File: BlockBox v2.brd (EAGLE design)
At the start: 199.4 x 119 mm, 367 parts, among them J100 TE-770966, J400 ICSP, J401 LED, J402 SWLED, J403 USB1, J404 USB2, J405 ZX62D-B-5PA8, J406 ZX62D-B-5PA8, J407 ZX62D-B-5PA8, J408 AUX, Q100 TK3R1E04PL, Q101 TK3R1E04PL, Q102 IPP052N06L3 G, Q103 IPP052N06L3 G, Q104 IPP052N06L3 G, Q105 IPP052N06L3 G, Q106 TK3R1E04PL, Q200 SUP90142E-GE3, Q201 SUP90142E-GE3, Q202 BUK9Y43-60E, Q203 DMP4065S, Q400 DMG2302UK, Q401 DMG2302UK, Q402 DMG2302UK, Q403 DMG2302UK, Q404 NMOS, Q405 NMOS, Q406 NMOS, SW100 PWRSW, SW400 VOL-, SW401 MFB, SW402 VOL+, SW403 BACK, SW404 PLAY, SW405 FWD, SW406 LCD_BL, SW407 LEDMODE, SW408 SDA01H1S, SW409 RESET, U100 BQ77915, U101 MAX1737, U102 LM74700-Q1, U103 LM74700-Q1, U104 LM74700-Q1, U200 LM5022, U201 LM3488, U202 LM25085, U203 TPS54308, U204 LD39150DT33, U300 TAS5548, U301 TAS5634, U302 NCS20071, U400 PIC32MZ-EF-100-I/PF, U401 FT230XS, U402 NCS4333, U403 FSAL200MTC, Y300 12.288MHz, Y400 12MHz

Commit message: Major PCB progress, about to shrink PCB (safety commit)
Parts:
- removed TP325, TP326: TPTP15R, testpad:TP15R
- moved U104 601.6 mm to (139.7, 2.54), flipped to the bottom, turned to 90 degrees
- moved U103 585.1 mm to (139.7, 14.0), flipped to the bottom, turned to 90 degrees
- moved TP102 579.4 mm to (96.5, -61.0)
- moved TP104 578.3 mm to (81.3, -61.0)
- moved TP105 578.3 mm to (74.9, -61.0)
- moved TP106 578.3 mm to (68.6, -61.0)
- moved R101 548.2 mm to (64.3, 14.0), flipped to the bottom, turned to 180 degrees
- moved D100 546.3 mm to (117.6, 13.6), turned to 270 degrees
- moved D102 544.5 mm to (83.8, 22.2), flipped to the bottom, turned to 180 degrees
- moved D101 544.0 mm to (112.0, 18.3), flipped to the bottom
- moved R127 543.0 mm to (92.8, 10.4), turned to 90 degrees
- moved R100 542.5 mm to (66.2, 18.0), flipped to the bottom, turned to 180 degrees
- moved R111 541.6 mm to (85.3, 14.5), turned to 180 degrees
- moved R107 540.1 mm to (72.8, 7.24), turned to 90 degrees
- moved R108 538.2 mm to (82.5, 11.4), turned to 90 degrees
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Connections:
- net AMP_!CLIP: now also TP310.TP; no longer TP326.TP
- net AMP_!OTW: now also TP309.TP; no longer TP325.TP
- net AMP_AVDD: no longer TP310.TP
- net AMP_DVDD: no longer TP309.TP
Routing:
- net VBAT: track 0.00 -> 160.8 mm, vias 0 -> 3
- net AMP_PVDD: track 0.00 -> 90.5 mm
- net CHG_CSSP: track 0.00 -> 81.6 mm, vias 0 -> 2
- net VSUP: track 0.00 -> 78.6 mm, vias 0 -> 2
- net VIN_EXT_FUSED: track 0.00 -> 73.8 mm, vias 0 -> 1
- net BAT-: track 0.00 -> 64.6 mm, vias 0 -> 9
- net CHG_CSSN: track 0.00 -> 64.2 mm, vias 0 -> 1
- net CHG_LX: track 0.00 -> 52.9 mm, vias 0 -> 1
- net BOOST_SW_DRAIN: track 0.00 -> 44.5 mm
- net 12V: track 0.00 -> 39.0 mm, vias 0 -> 1
- net CHG_!SHDN: track 0.00 -> 35.5 mm, vias 0 -> 1
- net BOOST_SW_GATE: track 0.00 -> 32.6 mm
- net DSP_XTALI: track 0.00 -> 28.7 mm
- net CHG_CS: track 0.00 -> 27.8 mm, vias 0 -> 3
- net BAT_THERM: track 0.00 -> 25.3 mm, vias 0 -> 2
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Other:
- board size 199.4 x 119 mm -> 141 x 119 mm

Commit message: Voltage converter layout done
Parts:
- moved R216 312.0 mm to (67.9, 40.3), flipped to the bottom
- moved R219 308.3 mm to (63.9, 41.5), flipped to the bottom, turned to 90 degrees
- moved U202 306.8 mm to (71.1, 40.6), flipped to the bottom, turned to 270 degrees
- moved C218 294.4 mm to (55.0, 31.9), turned to 270 degrees
- moved U203 294.4 mm to (66.2, 51.8), flipped to the bottom, turned to 270 degrees
- moved C215 288.0 mm to (67.9, 38.2), flipped to the bottom, turned to 180 degrees
- moved TP201 286.9 mm to (31.0, 79.4)
- moved C217 280.9 mm to (61.3, 40.4), flipped to the bottom, turned to 180 degrees
- moved R215 280.3 mm to (67.9, 44.3), flipped to the bottom
- moved C216 279.9 mm to (67.9, 42.3), flipped to the bottom, turned to 180 degrees
- moved U204 279.8 mm to (70.1, 50.4), turned to 270 degrees
- moved TP202 275.7 mm to (55.4, 36.6)
- moved L202 271.9 mm to (63.4, 39.9), turned to 180 degrees
- moved TP203 259.7 mm to (56.0, 58.0)
- moved C228 257.4 mm to (61.7, 60.2), flipped to the bottom, turned to 180 degrees
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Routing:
- net VSUP: track 78.6 -> 188.5 mm, vias 2 -> 6
- net 12V: track 39.0 -> 101.4 mm
- net 3.6V: track 0.00 -> 20.1 mm
- net SEPIC_SW_DRAIN: track 0.00 -> 18.9 mm, vias 0 -> 1
- net BUCK_FB: track 0.00 -> 17.7 mm, vias 0 -> 2
- net 5V: track 0.00 -> 16.4 mm, vias 0 -> 1
- net SEPIC_PREDIODE: track 0.00 -> 14.8 mm, vias 0 -> 1
- net SEPIC_SW_SOURCE: track 0.00 -> 13.9 mm, vias 0 -> 1
- net BUCK_SW_SOURCE: track 0.00 -> 9.32 mm
- net 3.3V: track 10.1 -> 18.7 mm
- net PRELIN_SW: track 0.00 -> 7.69 mm
- net SEPIC_COMP: track 0.00 -> 6.83 mm
- net SEPIC_FB: track 0.00 -> 6.07 mm
- net BUCK_SW_DRAIN: track 0.00 -> 5.70 mm, vias 0 -> 2
- net AMP_PVDD: track 90.5 -> 84.9 mm
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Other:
- board size 141 x 119 mm -> 124.5 x 119 mm

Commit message: PCB initially completed, final fixes
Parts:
- removed C417, C418, C419, C420: 0.1µF, rcl:C0603
- removed C421, C422: 18pF, rcl:C0603
- removed D401, D402, D403, D404: BAT60A, BW-Active:SOD323
- removed J407: ZX62D-B-5PA8, BW-Connectors:ZX62D-B-5PA8
- removed SJ403: FTRESET, jumper:SJ
- removed SJ404: USB-5V, jumper:SJ_2
- removed TP322, TP323, TP324, TP401, TP402, TP403, TP404, TP405, TP406, TP407: TPTP15R, testpad:TP15R
- added R411, R412: 10kΩ, resistor:R0603
- added R413, R414: 1kΩ, resistor:R0603
- added U404: NCS2333, BW-Active:MSOP8
- C401, C402, C403, C404, C407: value 15pF -> 0.1µF
- C405, C406: value 15pF -> 18pF
- SJ400: value USB -> USB-5V
- U400: value PIC32MZ-EF-100-I/PF -> PIC32MZ-EF-100
- U402: value NCS4333 -> NCS2333; device BW-Active:SO14 -> BW-Active:MSOP8
- moved R406 291.5 mm to (46.6, 59.2), turned to 180 degrees
- moved C411 284.0 mm to (41.4, 53.0), flipped to the bottom, turned to 270 degrees
- moved TP409 282.7 mm to (46.2, 45.5)
- moved TP411 279.8 mm to (24.3, 62.1), turned to 90 degrees
- moved C410 278.7 mm to (41.4, 49.9), flipped to the bottom, turned to 90 degrees
- moved TP408 274.5 mm to (43.7, 45.6)
- moved RV401 274.3 mm to (53.3, 41.1), turned to 180 degrees
- moved C407 271.7 mm to (49.5, 48.9), flipped to the bottom, turned to 270 degrees
- moved TP412 270.1 mm to (24.3, 56.1), turned to 90 degrees
- moved Q405 269.6 mm to (36.7, 28.7), flipped to the bottom
- moved SJ402 269.3 mm to (21.2, 68.3), flipped to the bottom, turned to 180 degrees
- moved SJ401 267.4 mm to (26.8, 35.2)
- moved R404 267.3 mm to (12.8, 23.6), flipped to the bottom, turned to 180 degrees
- moved C409 267.1 mm to (35.6, 49.5), flipped to the bottom
- moved Q404 266.1 mm to (40.8, 28.7), flipped to the bottom
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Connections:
- removed net BAT_CSN_BUF: R409.2, U402.8, U402.9
- removed net BAT_CSP_BUF: R408.2, U402.13, U402.14
- removed net FT_!RESET: SJ403.2, U401.11
- removed net MCU_USBID: J407.4, U400.56
- removed net MCU_USB_D+: J407.3, U400.55
- removed net MCU_USB_D-: J407.2, U400.54
- removed net MCU_USB_VBUS: J407.1, U400.51
- removed net MCU_VUSB3V3: SJ400.2, U400.52
- new net MCU_BAT_SENSE_BUF: C404.1, TP408.TP, U400.26, U404.6, U404.7
- new net MCU_BAT_SENSE_FB: R411.1, U402.1, U402.2
- new net MCU_CURR_SENSE_BUF: C403.1, TP409.TP, U400.27, U404.1, U404.2
- new net MCU_CURR_SENSE_FB: R407.1, R412.2, U402.7
- net 3.3V: now also C401.1, C402.1, C407.1, R413.2, R414.2, U402.8, U404.8; no longer C417.1, C418.1, C419.1, C420.1, D401.1, D402.1, SJ400.1, U402.4
- net 5V: now also SJ400.3; no longer SJ404.3
- net AMP_!CLIP: no longer TP310.TP
- net AMP_!FAULT: no longer TP324.TP
- net AMP_!OTW: no longer TP309.TP
- net AMP_!RESET: now also TP321.TP; no longer TP323.TP
- net BAT-: now also C402.2, U402.4; no longer U402.11
- net BAT_CSN: now also R409.2; no longer U402.10
- net BAT_CSP: now also R408.2; no longer U402.12
- net BM_ADAP_IN: now also SJ400.2; no longer SJ404.2
- net BM_USB_VBUS: now also SJ400.1; no longer SJ404.1
- net DSP_!BKND_ERR: now also TP310.TP; no longer TP322.TP
- net DSP_SCL: now also R414.1
- net DSP_SDA: now also R413.1
- net DSP_VALID: now also TP309.TP; no longer TP321.TP
- net GND: now also C401.2, C403.2, C404.2, C407.2, U400.52, U404.4; no longer C401.1, C402.1, C403.1, C404.1, C407.1, C417.2, C418.2, C419.2, C420.2, C421.1, C422.1, D403.2, D404.2, J407.5, J407.S1, J407.S2, J407.S3, J407.S4, SJ400.3, SJ403.1
- net LCD_!CS: no longer TP404.TP
- net LCD_!INT: no longer TP406.TP
- net LCD_!PD: no longer TP405.TP
- net LCD_BL_CTL: no longer TP407.TP
- net LCD_MISO: no longer TP402.TP
- net LCD_MOSI: no longer TP403.TP
- net LCD_SCK: no longer TP401.TP
- net MCU_BACK_SW: no longer C404.2
- net MCU_BAT_SENSE: now also R411.2, U404.5; no longer D401.2, D403.1, TP408.TP, U400.26, U402.1, U402.2
- net MCU_CURR_SENSE: now also R412.1, U404.3; no longer D402.2, D404.1, R407.1, TP409.TP, U400.27, U402.7
- net MCU_FWD_SW: no longer C402.2
- net MCU_LCD_BL_SW: no longer C401.2
- net MCU_MFB_SW: no longer C406.2
- net MCU_OSC1: now also C405.2; no longer C421.2
- net MCU_OSC2_R: now also C406.2; no longer C422.2
- net MCU_PLAY_SW: no longer C403.2
- net MCU_VOL+_SW: no longer C405.2
- net MCU_VOL-_SW: no longer C407.2
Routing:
- net 3.3V: track 18.7 -> 330.6 mm, vias 3 -> 19
- net 5V: track 16.4 -> 128.2 mm, vias 1 -> 3
- net I2S_LRCLK: track 0.00 -> 95.6 mm, vias 0 -> 4
- net I2S_SCLK: track 0.00 -> 91.6 mm, vias 0 -> 4
- net I2S_SD: track 0.00 -> 87.8 mm, vias 0 -> 5
- net 12V: track 101.4 -> 182.6 mm, vias 1 -> 3
- net MCU_!MCLR: track 0.00 -> 76.3 mm, vias 0 -> 4
- net MCU_CURR_SENSE: track 0.00 -> 75.5 mm
- net MCU_BAT_SENSE: track 0.00 -> 74.6 mm
- net MCU_PGD: track 0.00 -> 70.3 mm, vias 0 -> 4
- net MCU_PGC: track 0.00 -> 68.9 mm, vias 0 -> 4
- net DSP_EMO1: track 0.00 -> 64.5 mm
- net DSP_!RESET: track 0.00 -> 62.8 mm
- net DSP_!PDN: track 0.00 -> 61.3 mm
- net DSP_!BKND_ERR: track 0.00 -> 61.3 mm
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- added copper zone on layer 1, net GND
- added copper zone on layer 16, net GND
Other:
- board text added: "+"
- board text added: "-"
- board text added: "2"
- board text added: "<"
- board text added: ">"
- board text added: "BM83"
- board text added: "G"
- board text added: "LCD"
- board text added: "M"
- board text added: "MCU-USB"
- board text added: "POT"
- board text added: "UART"
- board text added: "USB"
- board text added: "||"

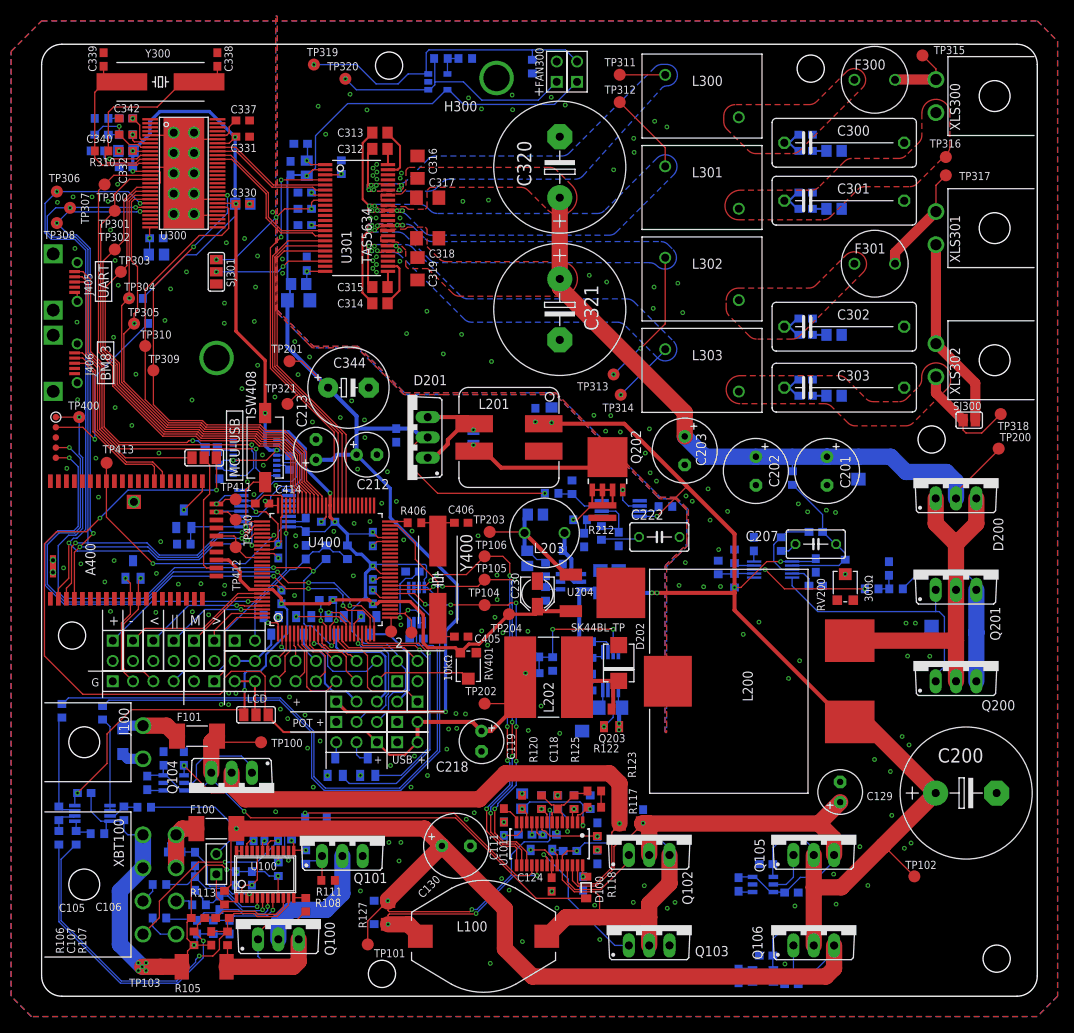
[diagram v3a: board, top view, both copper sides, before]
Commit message: Added logo and ground TPs
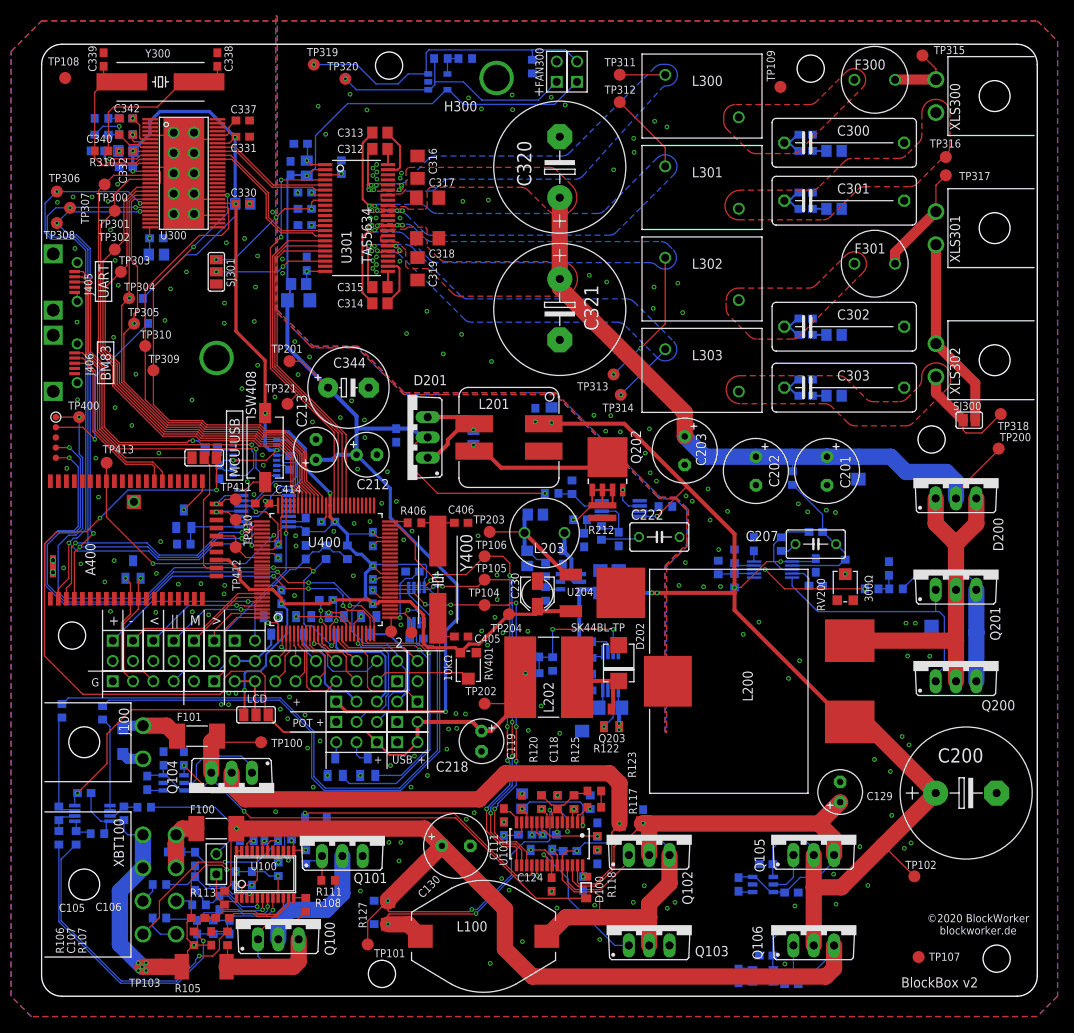
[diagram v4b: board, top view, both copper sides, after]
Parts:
- added TP107, TP108, TP109: TPTP15R, testpad:TP15R
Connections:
- net GND: now also TP107.TP, TP108.TP, TP109.TP
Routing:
- net GND: vias 247 -> 248
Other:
- board text added: "BlockBox v2"
- board text added: "©2020 BlockWorker blockworker.de"
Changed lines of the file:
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@@
 <wire x1="29.3624" y1="100.5586" x2="29.3624" y2="98.4758" width="0.8128" layer="29"/>
 <wire x1="30.099" y1="84.963" x2="33.909" y2="81.153" width="0.8128" layer="29"/>
-<wire x1="33.909" y1="81.153" x2="39.497" y2="81.153" width="0.8128" layer="29"/>
-<wire x1="39.497" y1="81.153" x2="45.3136" y2="75.3364" width="0.8128" layer="29"/>
-<wire x1="45.3136" y1="75.3364" x2="64.2366" y2="75.3364" width="0.8128" layer="29"/>
-<wire x1="64.2366" y1="75.3364" x2="67.2338" y2="72.3392" width="0.8128" layer="29"/>
 <wire x1="68.8848" y1="70.6882" x2="68.9102" y2="70.6628" width="0.8128" layer="29"/>
 <wire x1="74.1934" y1="65.3796" x2="77.2922" y2="62.2808" width="0.8128" layer="29"/>
 <wire x1="77.2922" y1="62.2808" x2="78.2828" y2="62.2808" width="0.8128" layer="29"/>
 <wire x1="79.6798" y1="61.8744" x2="80.7466" y2="60.8076" width="0.8128" layer="29"/>
-<wire x1="80.7466" y1="60.8076" x2="80.7466" y2="58.3438" width="0.8128" layer="29"/>
-<wire x1="80.6958" y1="56.4134" x2="78.0288" y2="53.7464" width="0.8128" layer="29"/>
 <wire x1="78.0288" y1="53.7464" x2="78.0288" y2="51.2318" width="0.8128" layer="29"/>
 <wire x1="78.0288" y1="49.6316" x2="78.0288" y2="43.2308" width="0.8128" layer="29"/>
 <wire x1="78.0288" y1="35.56" x2="78.0288" y2="33.1978" width="0.8128" layer="29"/>
 <wire x1="29.3624" y1="118.999" x2="29.3624" y2="102.6922" width="0.8128" layer="30"/>
-<wire x1="29.3624" y1="101.4984" x2="29.3624" y2="98.4758" width="0.8128" layer="30"/>
 <wire x1="29.3624" y1="94.0562" x2="29.3624" y2="91.5924" width="0.8128" layer="30"/>
 <wire x1="29.3624" y1="89.916" x2="29.3624" y2="88.4428" width="0.8128" layer="30"/>
@@
 <wire x1="8.763" y1="91.821" x2="6.731" y2="91.821" width="0.1524" layer="21"/>
 <text x="62.738" y="112.395" size="1.27" layer="21" font="vector" ratio="15" rot="R90">+</text>
+<polygon width="0.1524" layer="29">
+<vertex x="113.284" y="15.5702"/>
+<vertex x="116.332" y="15.5702"/>
+<vertex x="116.713" y="15.1892"/>
+<vertex x="116.713" y="13.6652"/>
+<vertex x="115.57" y="13.6652"/>
+<vertex x="115.951" y="14.0462"/>
+<vertex x="115.951" y="14.4272"/>
+<vertex x="115.57" y="14.8082"/>
+<vertex x="114.046" y="14.8082"/>
+<vertex x="114.046" y="10.9982"/>
+<vertex x="113.284" y="10.9982"/>
+</polygon>
+<polygon width="0.1524" layer="29">
+<vertex x="114.046" y="10.9982"/>
+<vertex x="116.332" y="10.9982"/>
+<vertex x="116.713" y="11.3792"/>
+<vertex x="116.713" y="12.9032"/>
+<vertex x="116.332" y="13.2842"/>
+<vertex x="116.713" y="13.6652"/>
+<vertex x="114.046" y="13.6652"/>
+<vertex x="114.046" y="12.9032"/>
+<vertex x="115.57" y="12.9032"/>
+<vertex x="115.951" y="12.5222"/>
+<vertex x="115.951" y="12.1412"/>
+<vertex x="115.57" y="11.7602"/>
+<vertex x="114.046" y="11.7602"/>
+</polygon>
+<polygon width="0.1524" layer="29">
+<vertex x="117.475" y="11.3792"/>
+<vertex x="117.856" y="10.9982"/>
+<vertex x="118.999" y="10.9982"/>
+<vertex x="119.38" y="11.3792"/>
+<vertex x="119.761" y="10.9982"/>
+<vertex x="120.904" y="10.9982"/>
+<vertex x="121.285" y="11.3792"/>
+<vertex x="121.285" y="15.1892"/>
+<vertex x="120.904" y="15.5702"/>
+<vertex x="120.523" y="15.5702"/>
+<vertex x="120.523" y="12.5222"/>
+<vertex x="120.142" y="12.1412"/>
+<vertex x="119.761" y="12.5222"/>
+<vertex x="119.761" y="15.1892"/>
+<vertex x="119.38" y="15.5702"/>
+<vertex x="118.999" y="15.1892"/>
+<vertex x="118.999" y="12.5222"/>
+<vertex x="118.618" y="12.1412"/>
+<vertex x="118.237" y="12.5222"/>
+<vertex x="118.237" y="15.5702"/>
+<vertex x="117.856" y="15.5702"/>
+<vertex x="117.475" y="15.1892"/>
+</polygon>
+<wire x1="113.284" y1="15.9512" x2="112.903" y2="15.5702" width="0.1524" layer="29"/>
+<wire x1="112.903" y1="15.5702" x2="112.903" y2="10.9982" width="0.1524" layer="29"/>
+<wire x1="112.903" y1="10.9982" x2="113.284" y2="10.6172" width="0.1524" layer="29"/>
+<wire x1="113.284" y1="10.6172" x2="121.285" y2="10.6172" width="0.1524" layer="29"/>
+<wire x1="121.285" y1="10.6172" x2="121.666" y2="10.9982" width="0.1524" layer="29"/>
+<wire x1="121.666" y1="10.9982" x2="121.666" y2="15.5702" width="0.1524" layer="29"/>
+<wire x1="121.666" y1="15.5702" x2="121.285" y2="15.9512" width="0.1524" layer="29"/>
+<wire x1="121.285" y1="15.9512" x2="113.284" y2="15.9512" width="0.1524" layer="29"/>
+<text x="117.0686" y="7.7216" size="1.016" layer="21" font="vector" ratio="15" align="bottom-center">©2020 BlockWorker
+blockworker.de</text>
+<text x="107.442" y="1.0922" size="1.27" layer="21" font="vector" ratio="15">BlockBox v2</text>
+<wire x1="33.909" y1="81.153" x2="35.7886" y2="81.153" width="0.8128" layer="29"/>
+<wire x1="44.1452" y1="76.5048" x2="45.3136" y2="75.3364" width="0.8128" layer="29"/>
+<wire x1="45.3136" y1="75.3364" x2="51.6382" y2="75.3364" width="0.8128" layer="29"/>
+<wire x1="65.2526" y1="74.3204" x2="67.183" y2="72.39" width="0.8128" layer="29"/>
+<wire x1="80.7466" y1="60.8076" x2="80.7466" y2="59.7662" width="0.8128" layer="29"/>
+<wire x1="78.0288" y1="53.7464" x2="79.3496" y2="55.0672" width="0.8128" layer="29"/>
 </plain>
 <attributes>
@@
 <attribute name="VALUE" x="10.668" y="83.1596" size="1.016" layer="28" font="vector" ratio="15" rot="MR0"/>
 </element>
+<element name="TP107" library="testpad" library_urn="urn:adsk.eagle:library:385" package="TP15R" package3d_urn="urn:adsk.eagle:package:27968/1" value="TPTP15R" x="109.6264" y="4.9022" smashed="yes">
+<attribute name="NAME" x="110.9083" y="4.4323" size="1.016" layer="25" font="vector" ratio="15"/>
+<attribute name="POPULARITY" value="0" x="109.6264" y="4.9022" size="1.27" layer="27" font="vector" ratio="15" display="off"/>
+<attribute name="TP_SIGNAL_NAME" value="BAT-" x="109.6264" y="2.3622" size="1" layer="37"/>
+</element>
+<element name="TP108" library="testpad" library_urn="urn:adsk.eagle:library:385" package="TP15R" package3d_urn="urn:adsk.eagle:package:27968/1" value="TPTP15R" x="2.9464" y="114.7826" smashed="yes">
+<attribute name="NAME" x="0.7993" y="116.3447" size="1.016" layer="25" font="vector" ratio="15"/>
+<attribute name="POPULARITY" value="0" x="2.9464" y="114.7826" size="1.27" layer="27" font="vector" ratio="15" display="off"/>
+<attribute name="TP_SIGNAL_NAME" value="BAT-" x="2.9464" y="112.2426" size="1" layer="37"/>
+</element>
+<element name="TP109" library="testpad" library_urn="urn:adsk.eagle:library:385" package="TP15R" package3d_urn="urn:adsk.eagle:package:27968/1" value="TPTP15R" x="92.3544" y="113.665" smashed="yes">
+<attribute name="NAME" x="91.6559" y="114.3373" size="1.016" layer="25" font="vector" ratio="15" rot="R90"/>
+<attribute name="POPULARITY" value="0" x="92.3544" y="113.665" size="1.27" layer="27" font="vector" ratio="15" display="off"/>
+<attribute name="TP_SIGNAL_NAME" value="BAT-" x="92.3544" y="111.125" size="1" layer="37"/>
+</element>
 </elements>
 <signals>
@@
 <via x="60.7822" y="45.6184" extent="1-16" drill="0.3"/>
 <via x="62.4332" y="36.2712" extent="1-16" drill="0.3"/>
+<contactref element="TP107" pad="TP"/>
+<contactref element="TP108" pad="TP"/>
+<contactref element="TP109" pad="TP"/>
+<via x="32.0294" y="100.457" extent="1-16" drill="0.3"/>
 </signal>
 <signal name="BAT-_INT2">
@@
 </drawing>
 <compatibility>
+<note version="6.3" minversion="6.2.2" severity="warning">
+Since Version 6.2.2 text objects can contain more than one line,
+which will not be processed correctly with this version.
+</note>
 <note version="8.2" severity="warning">
 Since Version 8.2, EAGLE supports online libraries. The ids
